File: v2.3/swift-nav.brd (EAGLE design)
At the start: 53 x 53 mm, 171 parts, among them J1 SMA_EDGE, J6 ZX62-B-5PA, Q1 IRLML6401, U1 6SLX9FTG256, U10 MAX2769, U12 PT7M8206B33TA5EX, U13 M25PX80, U2 LTC3407A_DFN, U3 STM32-M-64-LQFP, U4 7Q-16.368MBG-T, U5 SMA_PATCH, U6 93LC56BT-I/OT, U7 FT232HQ, U8 B4050, X4 NX5032GA-12M, X5 CONN_5-2

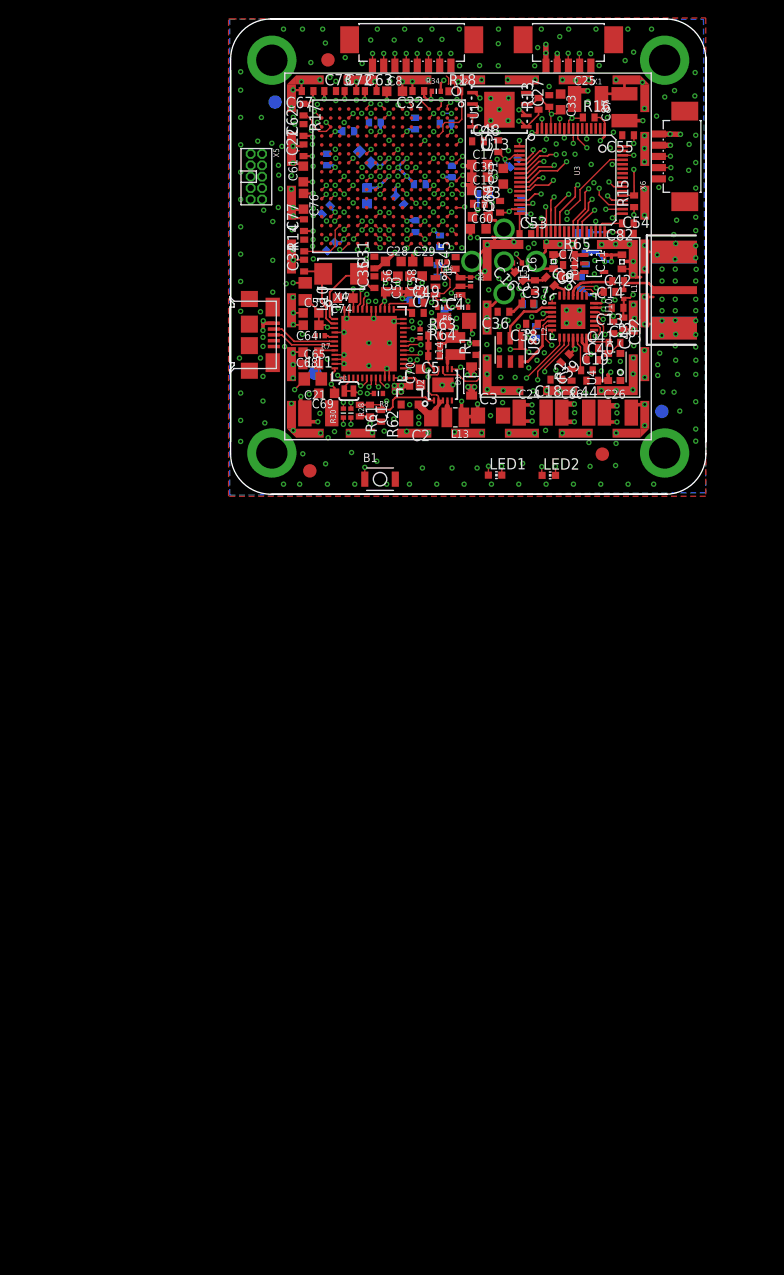
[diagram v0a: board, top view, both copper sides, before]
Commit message: In schematic: -Resistor between V_USB and STM USB detect pin -Add more FIFO lines from FPGA -Removed internal shield -Added LNA and associated components to LNA1 line -Changed LNA1 SMA to 1 thru hole signal 4 SMD GND pads -Changed digital supplies on MAX (TCXO, ADC, VDD_D) to digital 3V3 In board: -Changed patch position to center of board
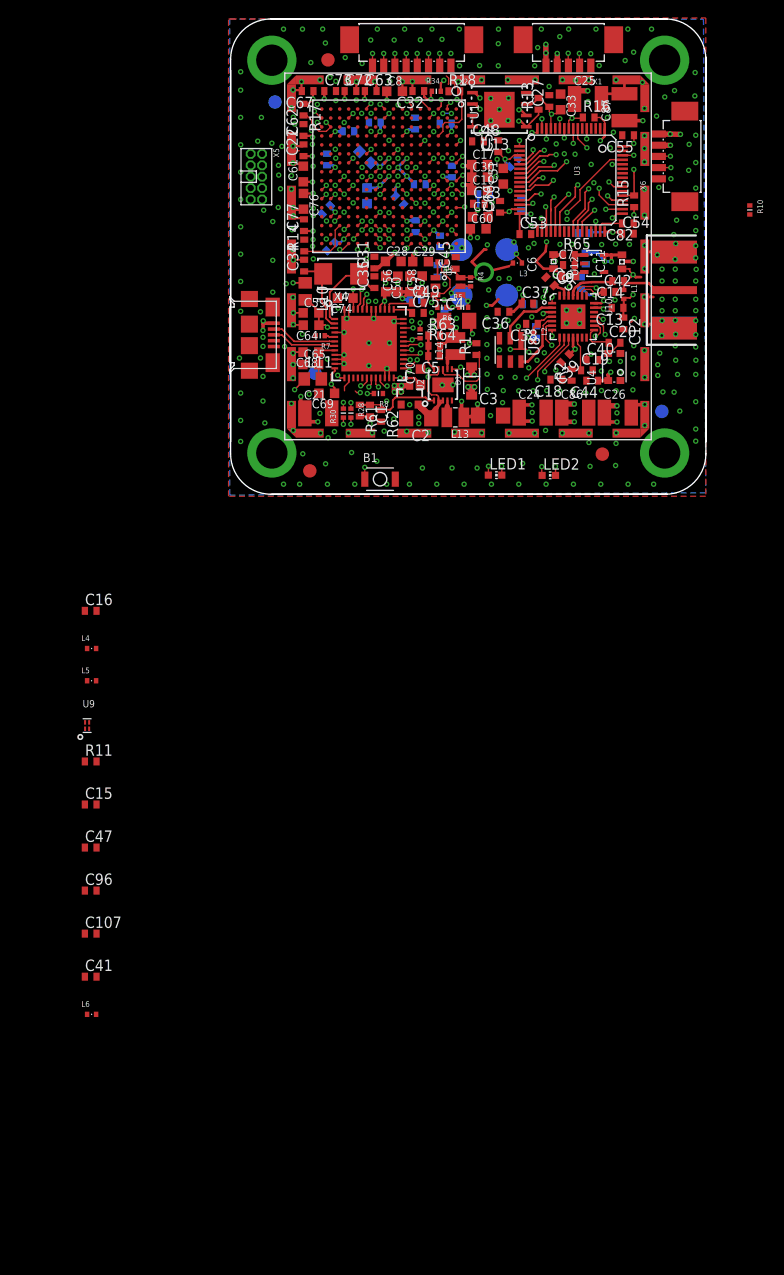
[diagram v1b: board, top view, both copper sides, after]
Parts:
- removed C43: 0.47uF, rcl:C0402
- removed SHLD1: BMI-S-202, jobygnss:BMI-S-202
- removed SJ1: SOLDERJUMPERTRACE, SparkFun-Passives:SJ_2S-TRACE
- added C107, C96: 0.47uF, rcl:C0402
- added C47: 100pF, rcl:C0402
- added L4: 3.3nH, pel_dipol_comp:0402-IND
- added L5: 5.1nH, pel_dipol_comp:0402-IND
- added L6: 36nH, pel_dipol_comp:0402-IND
- added R10: 10K, pel_dipol_comp:0402-RES
- added R11: 600, rcl:R0402
- added U9: XC2401, swift-nav:XC2401
- C15: value DNP -> 0.047uF
- C16: value 0R -> 100pF
- C41: value 0.47uF -> 12pF
- U5: value SMA_PATCH -> SMA_PATCH_SMDGND; device joby_robotics:SMA_PATCH -> joby_robotics:SMA_PATCH_SMDGND
- moved C41 89.7 mm to (-12.2, -50.4)
- moved C15 76.1 mm to (-12.2, -31.2), turned to 0 degrees
- moved C16 60.6 mm to (-12.2, -9.60), turned to 0 degrees
- moved U5 2.52 mm to (29.9, 29.9)
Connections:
- removed net UART6_RX: U3.38, U7.13
- removed net UART6_TX: SJ1.2, U3.37
- new net FTDI_ADBUS2: U1.T15, U7.15
- new net FTDI_ADBUS3: U1.R15, U7.16
- new net FTDI_ADBUS4: U1.P16, U7.17
- new net N$18: R10.P$1, U3.26
- new net N$36: C95.1, U9.2
- new net N$37: C15.2, C47.2, L6.P$2, R11.1
- new net N$38: U10.13
- new net N$41: C41.2, L6.P$1, U9.1
- new net N$42: C107.1, C96.1
- new net UART6_RX/FTDI_ADBUS0: U1.H15, U3.38, U7.13
- new net UART6_TX/FTDI_ADBUS1: U1.G16, U3.37, U7.14
- net GND: now also C107.2, C41.1, C47.1, C96.2, L4.P$1, U5.2, U5.3, U5.4, U5.5, U9.3; no longer C41.2, C43.2, SHLD1.1, SHLD1.10, SHLD1.11, SHLD1.12, SHLD1.2, SHLD1.3, SHLD1.4, SHLD1.5, SHLD1.6, SHLD1.7, SHLD1.8, SHLD1.9, U5.P2, U5.P3, U5.P4, U5.P5
- net N$14: now also C16.1, U5.1; no longer C16.2, U5.P1
- net N$2: now also L5.P$1, U9.4; no longer SJ1.1, U7.14
- net N$35: now also C16.2, L4.P$2, L5.P$2; no longer C15.2, C16.1, C95.1
- net VCC: now also R11.2; no longer C41.1, C43.1, C44.1, U10.13, U10.14, U10.19, U4.4
- net VCCIO: now also C44.1, U10.14, U10.19, U4.4
- net V_USB: now also R10.P$2; no longer U3.26
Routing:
- net UART6_TX/FTDI_ADBUS1: track 0.00 -> 52.8 mm, vias 0 -> 2
- net UART6_RX/FTDI_ADBUS0: track 0.00 -> 51.6 mm, vias 0 -> 2
- net UART6_RX: track 51.6 -> 0.00 mm, vias 2 -> 0
- net UART6_TX: track 51.3 -> 0.00 mm, vias 2 -> 0
- net GND: track 91.9 -> 81.5 mm, vias 398 -> 396
- net VCC: track 30.4 -> 21.7 mm, vias 9 -> 7
- net N$35: track 2.65 -> 0.00 mm
- net VCCIO: track 160.9 -> 163.4 mm, vias 74 -> 75
- net N$2: track 1.67 -> 0.00 mm
- net N$14: track 2.30 -> 3.46 mm
- net V_USB: track 133.0 -> 131.9 mm

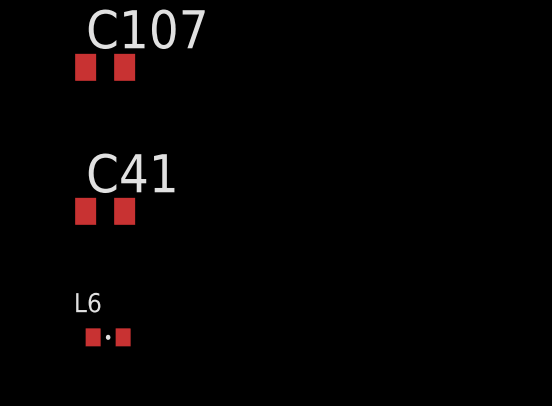
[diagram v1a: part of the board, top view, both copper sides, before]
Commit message: Cleaned up RF section a little bit. Going to split MAX2769 symbol up a little bit more to clean it up further.
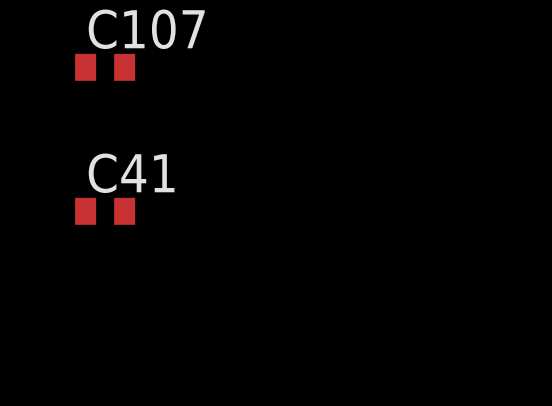
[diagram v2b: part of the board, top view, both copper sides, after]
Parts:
- removed L6: 36nH, pel_dipol_comp:0402-IND
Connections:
- removed net N$37: C15.2, C47.2, L6.P$2, R11.1
- removed net N$42: C107.1, C96.1
- net N$41: now also C15.2, C47.2, R11.1; no longer L6.P$1
- net VCCIO: now also C107.1, C96.1

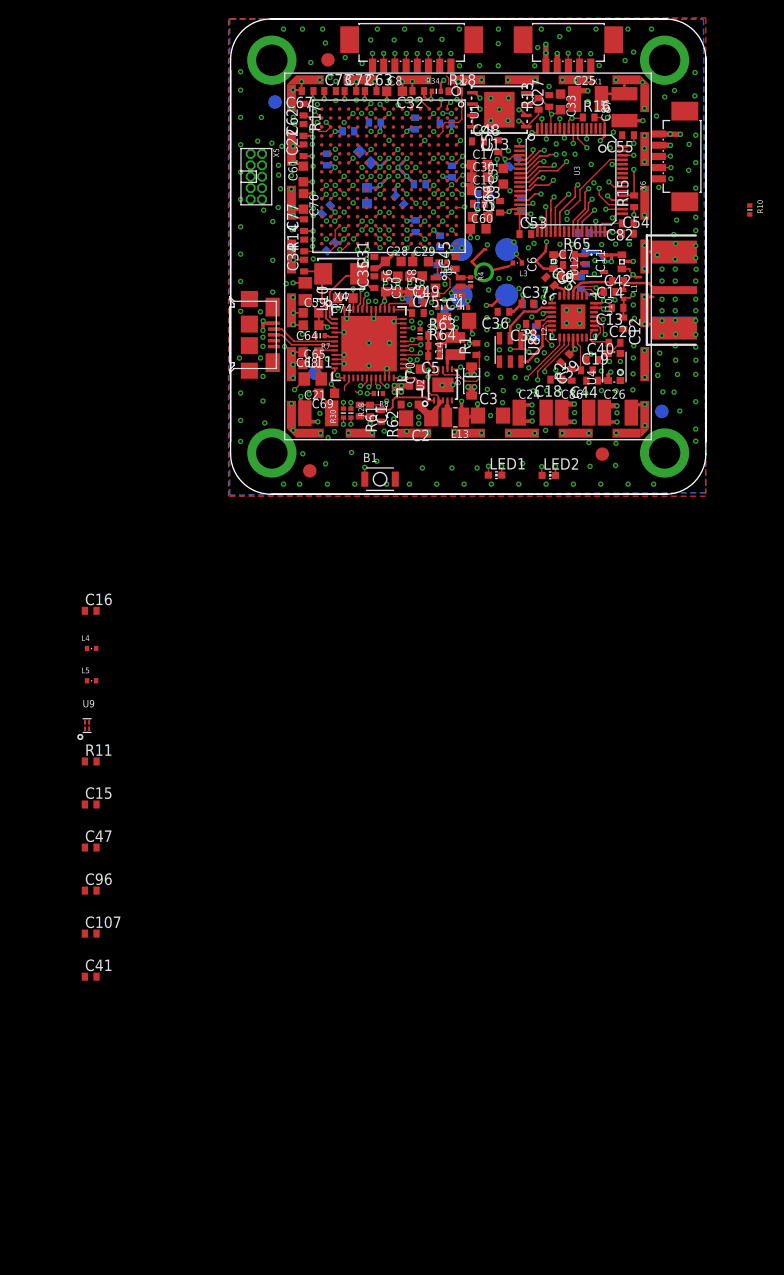
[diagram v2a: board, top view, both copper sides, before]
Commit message: Cleaned up RF section a bit more - separated max2769 into 3 symbols
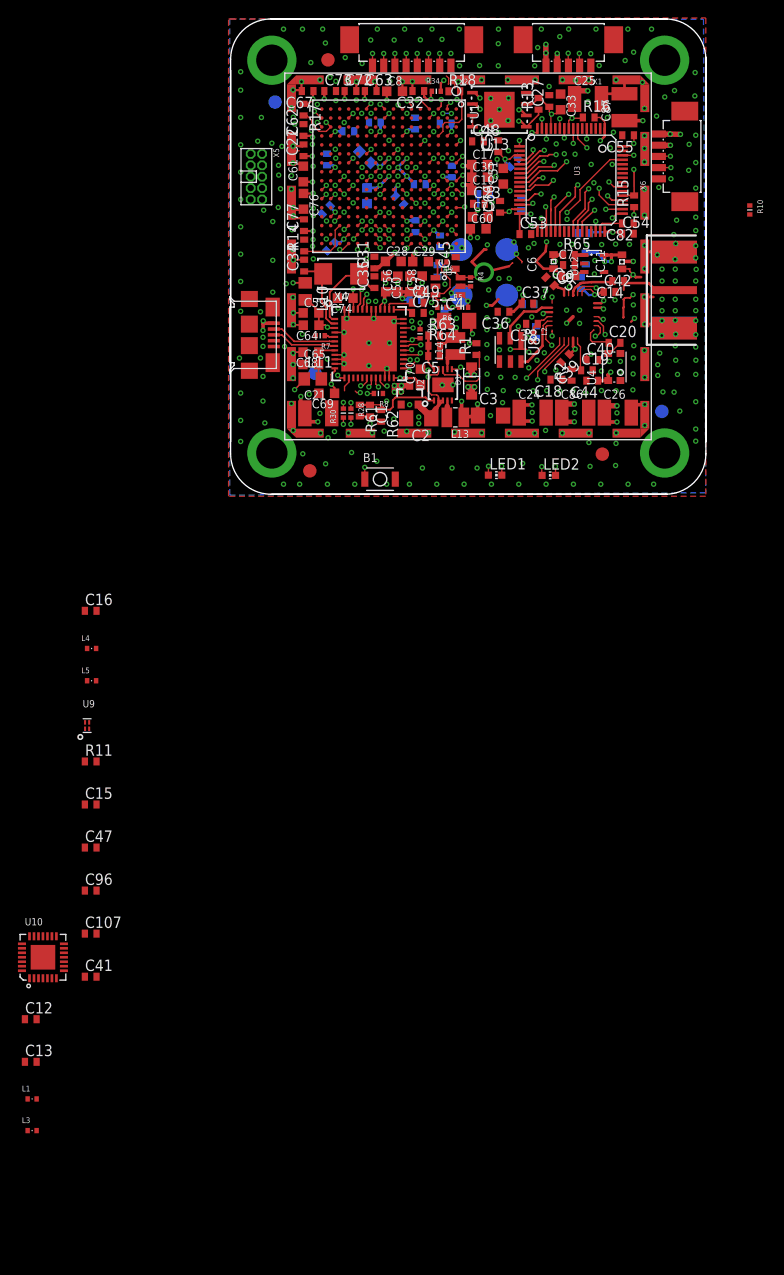
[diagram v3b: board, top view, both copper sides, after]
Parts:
- L1: value 250nH -> 29nH
- L2: value 36nH -> 29nH
- L3: value 250nH/DNP -> 29nH
- moved L1 111.4 mm to (-18.7, -64.0), turned to 0 degrees
- moved L3 110.9 mm to (-18.7, -67.6), turned to 0 degrees
- moved C13 106.5 mm to (-18.9, -59.9), turned to 0 degrees
- moved C12 101.9 mm to (-18.9, -55.1), turned to 0 degrees
- moved U10 92.7 mm to (-17.5, -48.2), turned to 0 degrees
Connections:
- removed net N$10: C12.1, C13.1, L1.P$2, L3.P$1, U10.3
- removed net N$38: U10.13
- new net N$37: C12.2, C13.2, L1.P$1, L3.P$2, U10.3
- net GND: now also C12.1, C13.1; no longer C12.2, C13.2
- net N$14: now also L1.P$2; no longer L3.P$2
- net N$8: now also L3.P$1; no longer L1.P$1
- net VCC: now also U10.13

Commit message: Added pull up resistors to NIDLE and NSHDN and pull down to PGM
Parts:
- removed C41: 12pF, rcl:C0402
- added R12, R19, R20: 10k, rcl:R0402
- moved U10 92.7 mm to (41.6, 23.2), turned to 270 degrees
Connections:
- net GND: now also R20.1; no longer C41.1
- net MAX_NIDLE: now also R12.1
- net MAX_NSHDN: now also R19.1
- net MAX_PGM: now also R20.2
- net N$41: no longer C41.2
- net VCCIO: now also R12.2, R19.2

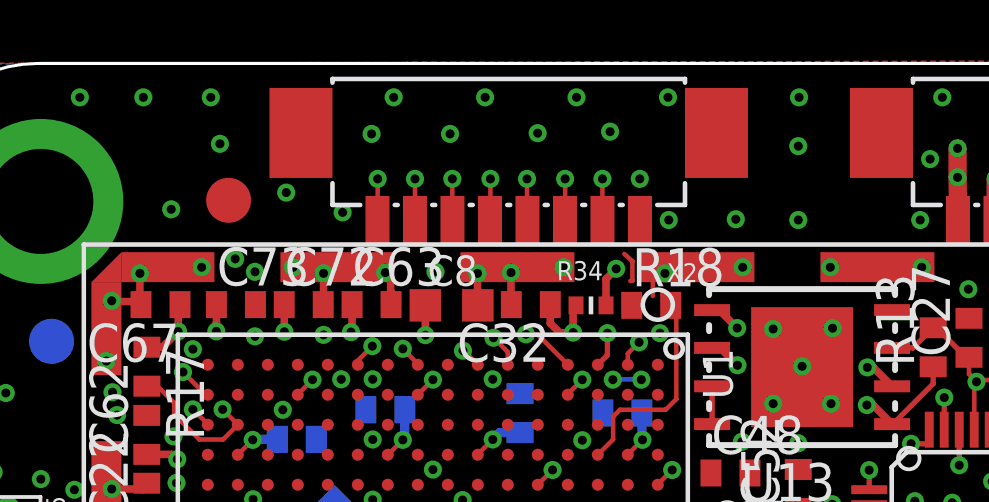
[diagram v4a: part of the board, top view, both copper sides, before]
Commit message: Changed debug header to 12 pin with 1 gnd 1 VDD and 10 signal connections
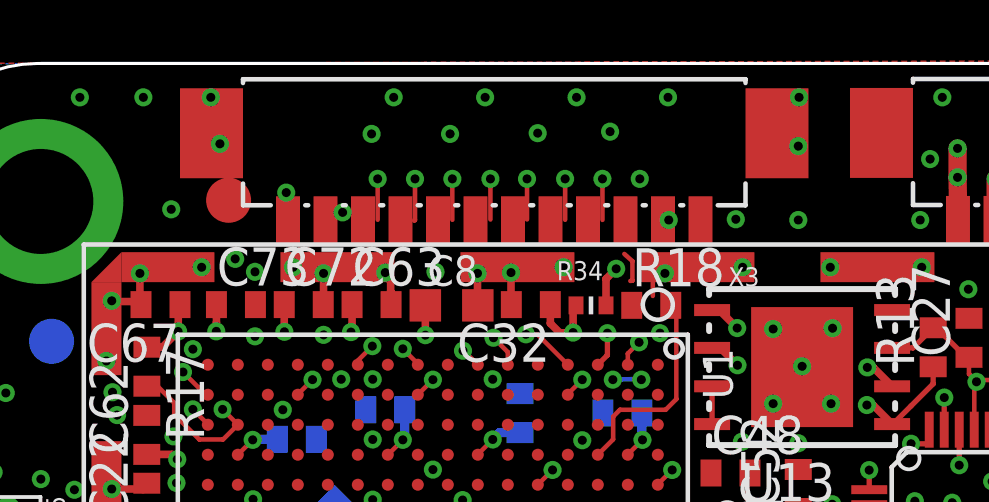
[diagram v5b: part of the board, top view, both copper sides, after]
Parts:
- removed X2: (no value), pel_molex:PB-53261-08
- added X3: FPGA DEBUG, pel_molex:PB-53261-12
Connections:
- new net DEBUG7: X3.4
- new net DEBUG8: X3.3
- new net DEBUG9: X3.2
- net DEBUG0: now also X3.11; no longer X2.8
- net DEBUG1: now also X3.10; no longer X2.7
- net DEBUG2: now also X3.9; no longer X2.6
- net DEBUG3: now also X3.8; no longer X2.5
- net DEBUG4: now also X3.7; no longer X2.4
- net DEBUG5: now also X3.6; no longer X2.3
- net DEBUG6: now also X3.5; no longer X2.2
- net GND: now also X3.1; no longer X2.1
- net VDD: now also X3.12

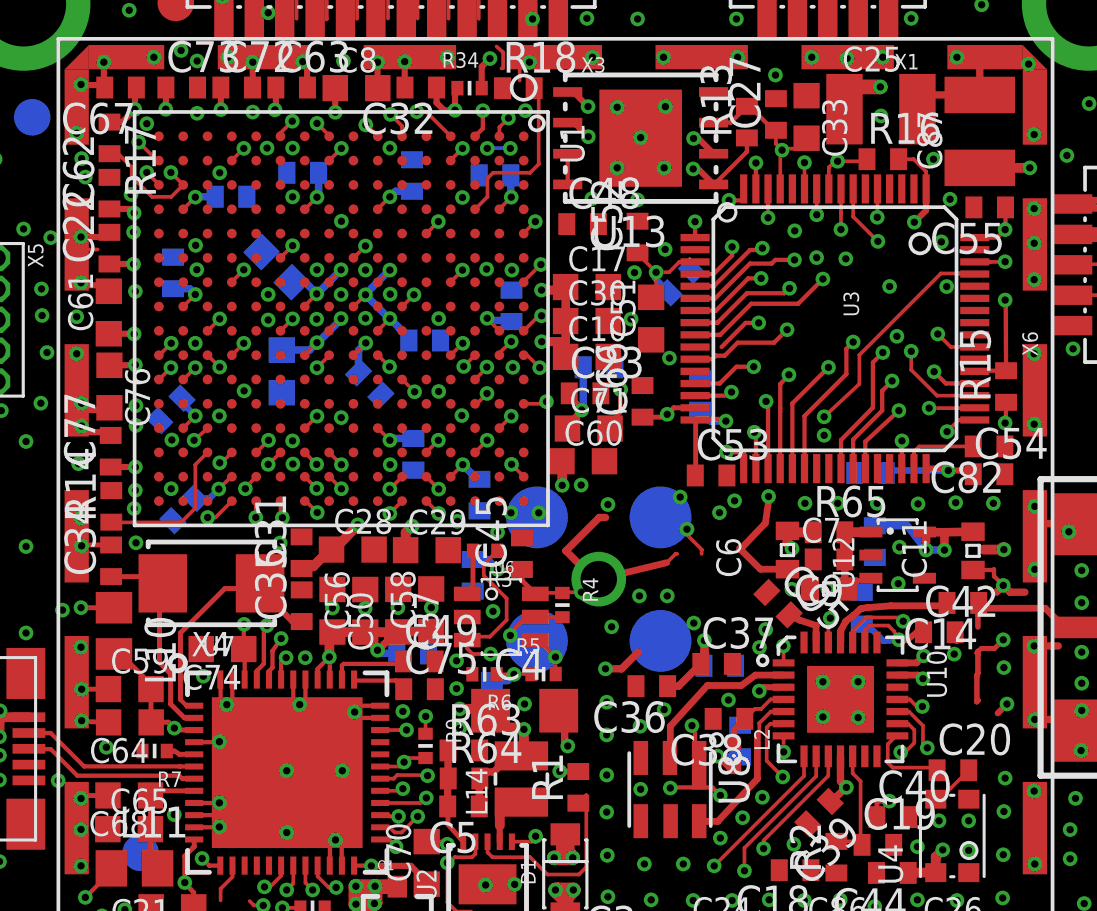
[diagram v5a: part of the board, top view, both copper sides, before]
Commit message: Removed capacitors from bottom of board
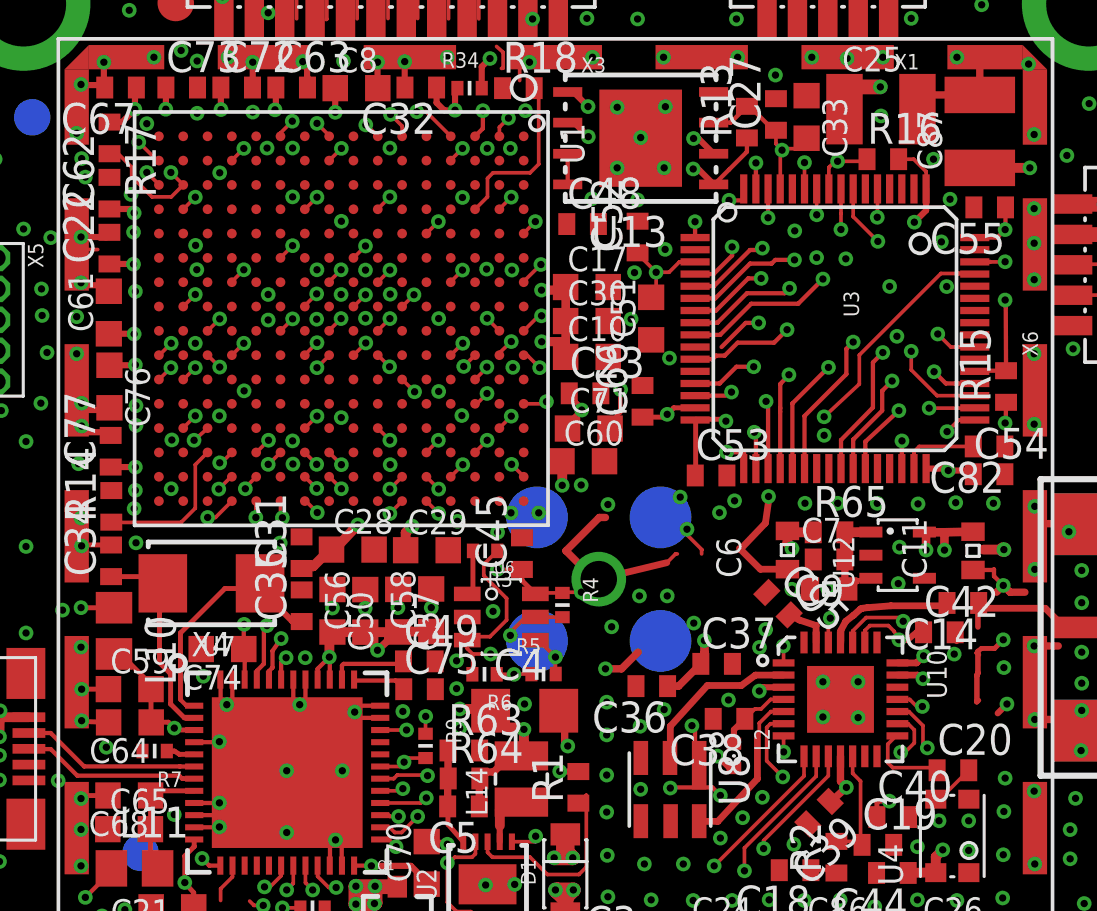
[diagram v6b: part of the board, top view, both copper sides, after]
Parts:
- removed C100, C101, C102, C103, C104, C105, C106, C78, C80, C81, C83, C84, C85, C88, C89, C90, C91, C92, C93, C94, C97, C98, C99: 0.47uF, rcl:C0402
- removed C46, C79: 4.7uF, rcl:C0603K
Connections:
- net GND: no longer C100.2, C101.2, C102.2, C103.2, C104.2, C105.2, C106.2, C46.2, C78.2, C79.2, C80.2, C81.2, C83.2, C84.2, C85.2, C88.2, C89.2, C90.2, C91.2, C92.2, C93.2, C94.2, C97.2, C98.2, C99.2
- net VCC: no longer C91.1, C92.1, C93.1, C94.1
- net VCCINT: no longer C46.1, C78.1, C79.1, C80.1
- net VCCIO: no longer C100.1, C101.1, C102.1, C103.1, C104.1, C105.1, C106.1, C81.1, C83.1, C84.1, C85.1, C88.1, C89.1, C90.1, C97.1, C98.1, C99.1
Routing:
- net VCCIO: track 163.4 -> 143.7 mm
- net VCCINT: track 87.2 -> 76.1 mm
- net VCC: track 21.7 -> 14.3 mm
- net GND: track 81.5 -> 80.4 mm
